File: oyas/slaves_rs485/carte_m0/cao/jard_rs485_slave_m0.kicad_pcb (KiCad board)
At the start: 2 copper layers, 78.6 x 30 mm, 69 parts, among them J1 POWER, J2 Niveaux/Débit, J3 EV1, J4 ISCP, Q1 BPC_FMMT38C, Q2 P03P4L-04, U1 BPC_Alim5V, U2 ATSAMD21G18A-A, U3 MAX3485, U4 AP1117-15

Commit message: Finitions PCB
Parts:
- D9: footprint Package_TO_SOT_SMD:SOT-23 -> bpc:BPC_SOT-23-3_HandSoldering
- Q1: footprint bpc:BPC_SOT-23-3 -> bpc:BPC_SOT-23-3_HandSoldering
- TP3: value H -> High
- TP4: value L -> Low
- TP8: value C -> Cmd
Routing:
- net +3.3V: track 251.3 -> 272.7 mm, vias 9 -> 10
- net POWER_12V: track 27.6 -> 26.6 mm
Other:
- board text added: "0"
- board text added: "Oya"
- board text added: "Pompe"
- board text added: "Slave Oya M0 Rev A / 2026"
- board text removed: "Slave Oya MSP430 Rev B / 2025"

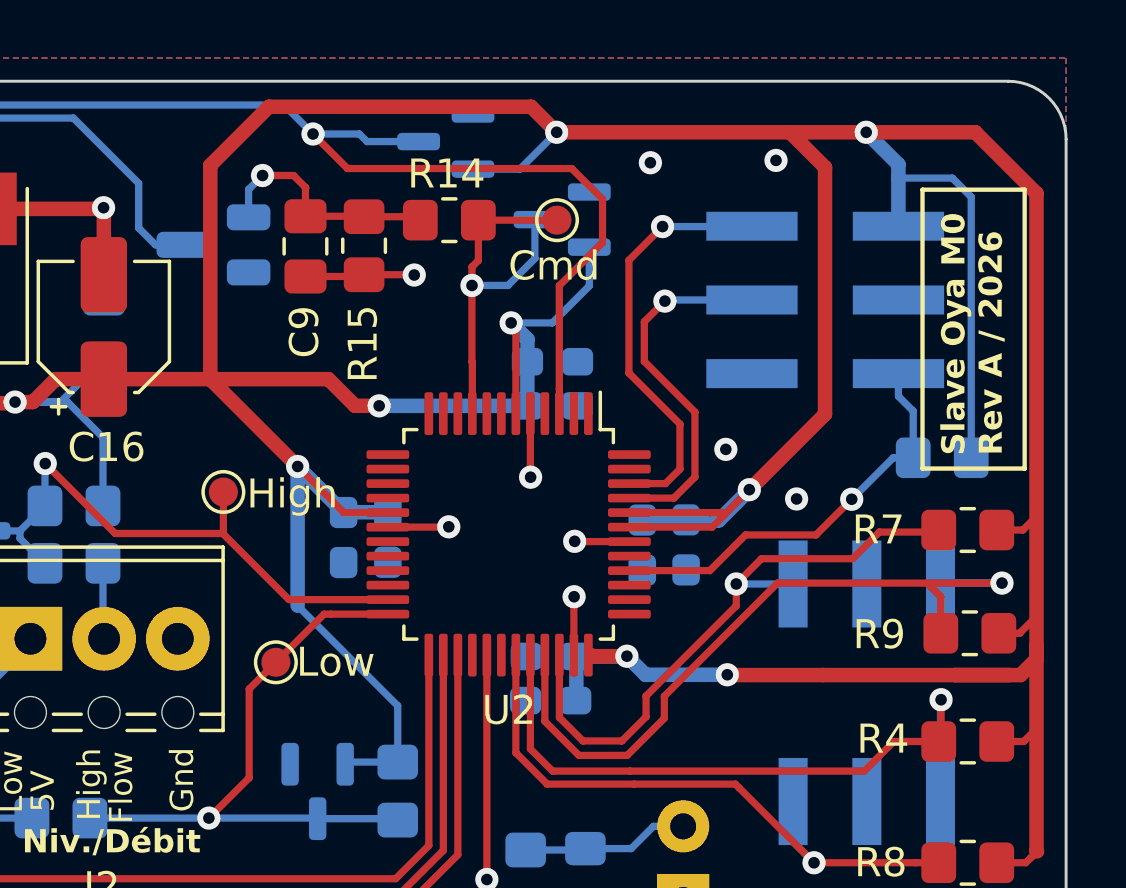
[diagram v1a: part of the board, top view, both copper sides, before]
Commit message: Revue de carte et de routage:
- Amélioration découplage micro (1uF 805 sur VDDCore et 100nF 603 sur les autres selon recommendation microchip)
- R14=1k: Moins de courant dans Q1
- R1=R2=1k: Limiter le clamp en mode débit
- R3 NM en mode débit
- C17=100nF pour améliorer filtrage 3.3V
- Ajout Capa 100nF sur reset
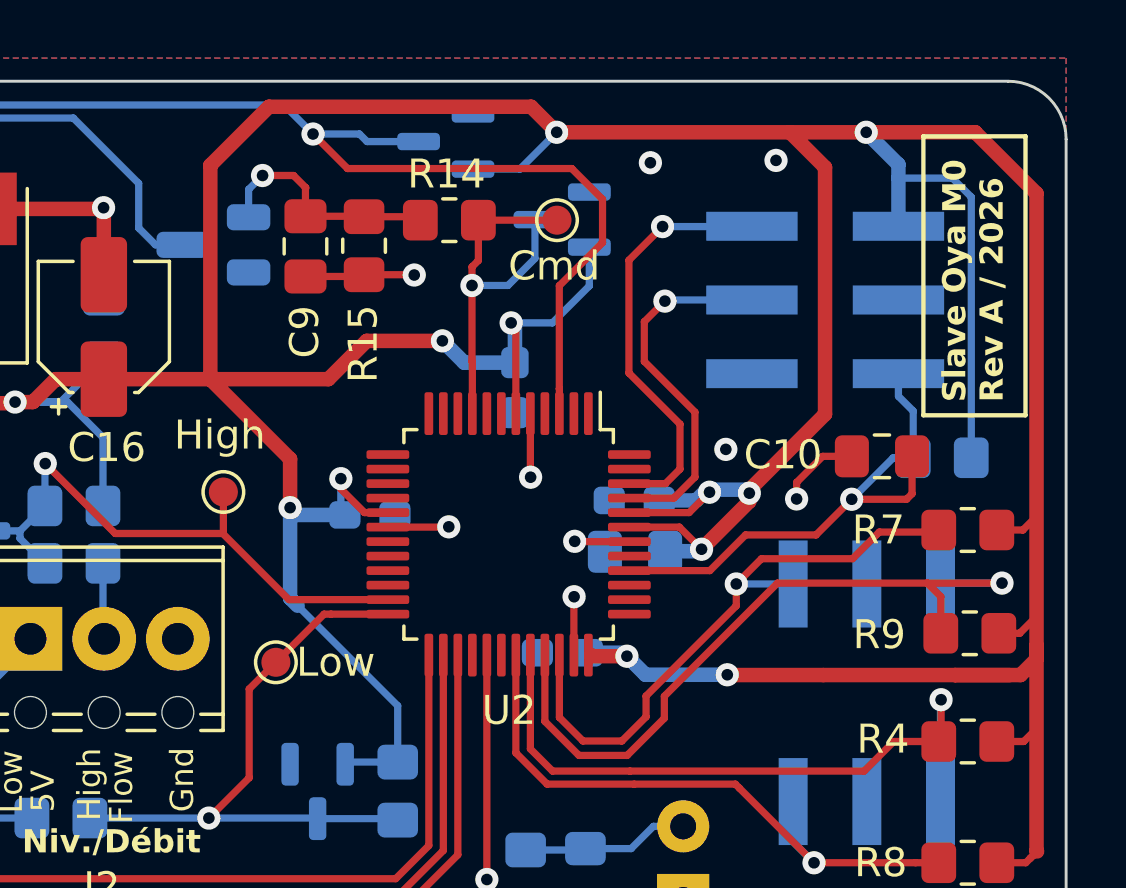
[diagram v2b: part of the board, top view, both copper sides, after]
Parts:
- removed C12: 1µF, Capacitor_SMD:C_0603_1608Metric_Pad1.08x0.95mm_HandSolder
- removed C14: 1nF, Capacitor_SMD:C_0603_1608Metric_Pad1.08x0.95mm_HandSolder
- C10: value 1µF -> 100nF; footprint Capacitor_SMD:C_0603_1608Metric_Pad1.08x0.95mm_HandSolder -> Capacitor_SMD:C_0805_2012Metric_Pad1.18x1.45mm_HandSolder; moved to F.Cu
- C11, C15, C17, C5: value 1nF -> 100nF
- C13: footprint Capacitor_SMD:C_0603_1608Metric_Pad1.08x0.95mm_HandSolder -> Capacitor_SMD:C_0805_2012Metric_Pad1.18x1.45mm_HandSolder
- C4: value 1µF -> 100nF
- R1, R2: value 100 -> 1k
- R14: value 220 -> 1k
- moved C10 17.3 mm to (185.7, 99.7), turned to 0 degrees
- moved C4 4.31 mm to (177.1, 101.2)
- moved C5 1.57 mm to (173.0, 97.4), turned to 90 degrees
- moved C11 1.19 mm to (168.0, 101.8), turned to 180 degrees
- moved C15 0.40 mm to (174.6, 106.5)
- moved C13 0.34 mm to (177.1, 103.0), turned to 180 degrees
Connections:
- C10 pad 2: +3.3V -> /RESET
- C4 pad 1: GND -> +3.3V
- C4 pad 2: +3.3V -> GND
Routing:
- net +3.3V: track 272.7 -> 267.4 mm, vias 10 -> 13
- net /RESET: track 14.5 -> 18.0 mm
- net GND: track 46.8 -> 49.7 mm

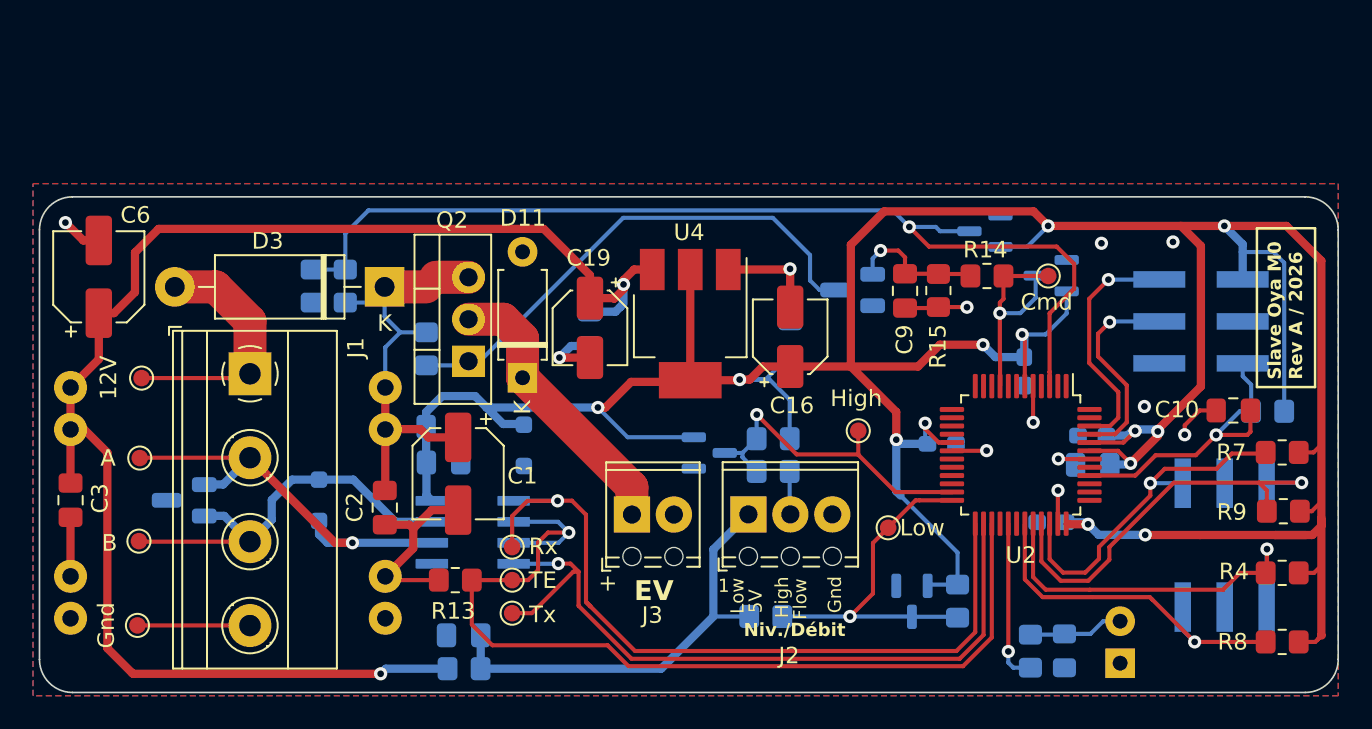
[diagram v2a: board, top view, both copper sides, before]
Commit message: Fin de revue avec ajout d'une diode TVS 18V en entrée
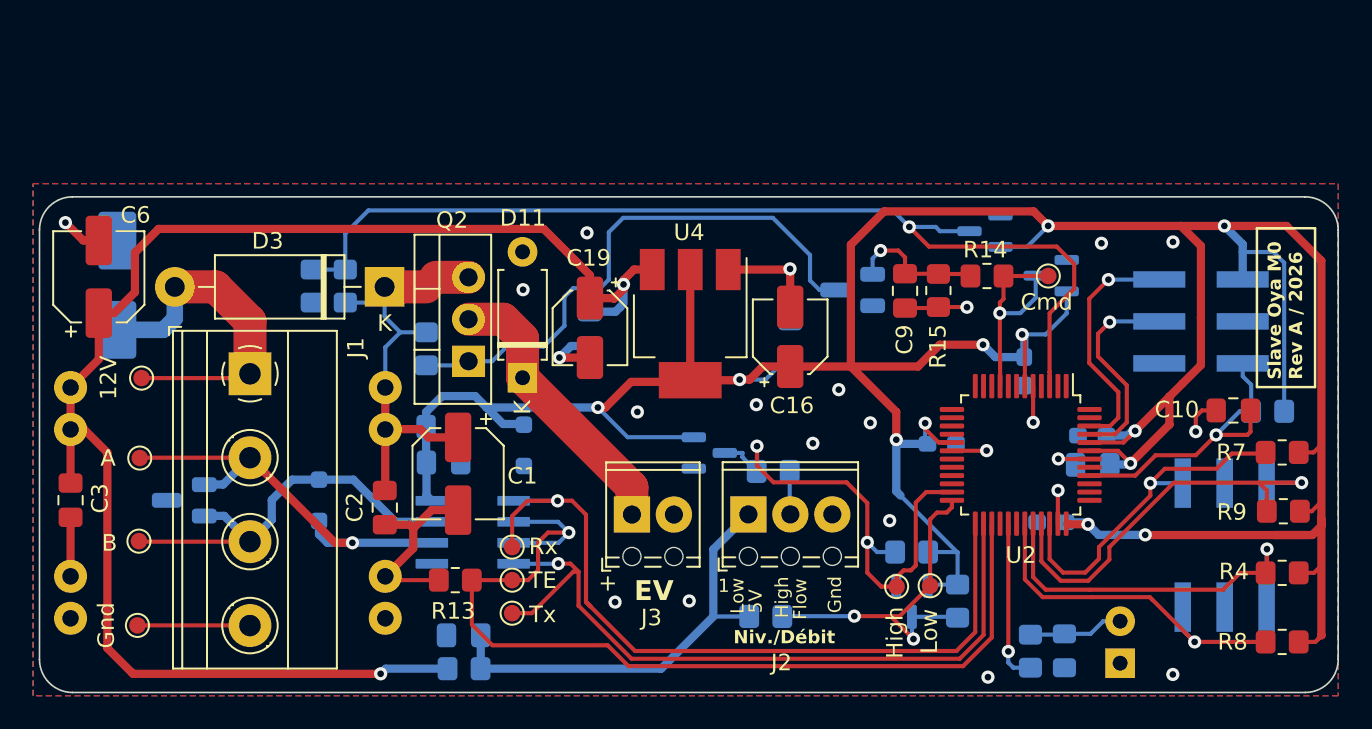
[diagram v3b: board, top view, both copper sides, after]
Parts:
- added D12: SMBJ18A, Diode_SMD:D_SMB_Handsoldering, B.Cu at (118.1, 92.2)
- moved R3 10.8 mm to (166.2, 108.3)
- moved TP3 9.71 mm to (165.3, 110.4)
- moved TP4 4.33 mm to (167.3, 110.3)
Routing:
- net LVL_HIGH_FLOW: track 20.4 -> 29.4 mm, vias 1 -> 2
- net Net-(D12-A1): track 15.3 -> 20.9 mm
- net Net-(Q1-C): track 31.2 -> 33.9 mm
- net +3.3V: track 267.4 -> 264.8 mm, vias 13 -> 12
- net GND: track 49.7 -> 49.1 mm, vias 12 -> 23
- net LVL_LOW: track 21.5 -> 21.9 mm, vias 1 -> 2

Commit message: Préparation future carte Rev B (Inversion TX/RX) Programme en cours de test
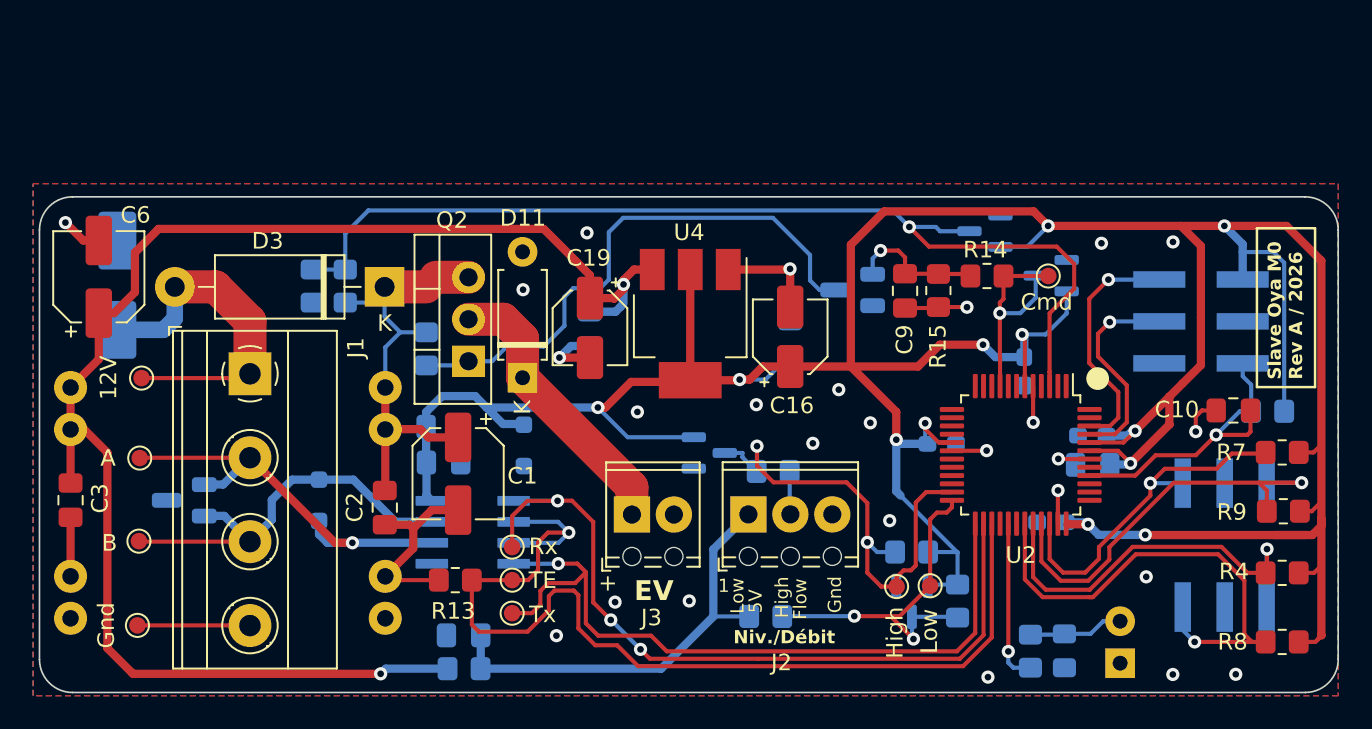
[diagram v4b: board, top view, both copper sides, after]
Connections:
- U2 pad 25: RX -> TX
- U2 pad 26: TX -> RX
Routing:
- net A3: track 21.9 -> 29.7 mm
- net TX_EN: track 58.1 -> 61.8 mm
- net A1: track 23.0 -> 24.3 mm
- net TX: track 44.4 -> 45.0 mm
- net RX: track 47.2 -> 47.6 mm, vias 1 -> 3
- net GND: vias 23 -> 26

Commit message: Amélioration pad de R10 Sortie du module adc Calibration de la mesure d'alim
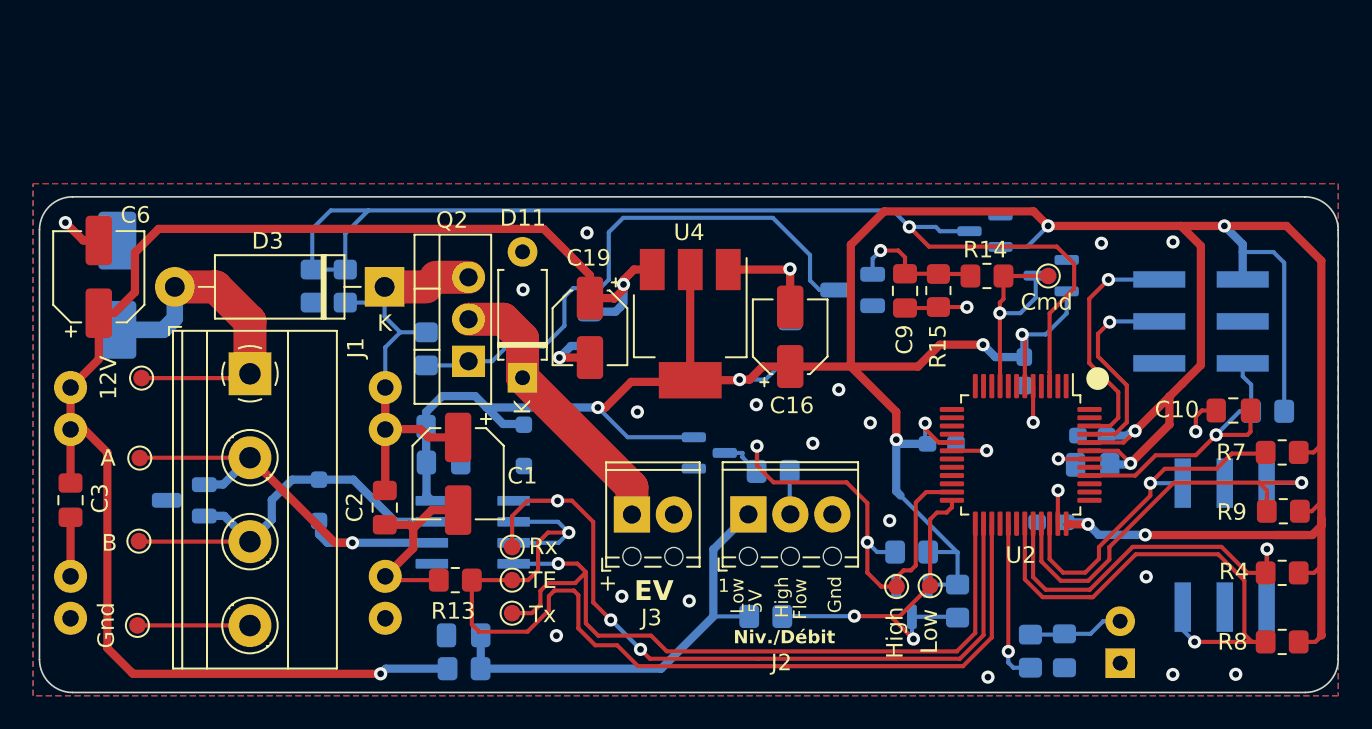
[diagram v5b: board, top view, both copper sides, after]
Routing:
- net POW_MES: track 62.0 -> 68.3 mm
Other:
- board text removed: "Slave Oya M0 Rev A / 2026"
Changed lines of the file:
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@@
   (gr_circle (center 144.06 104.71) (end 143.76 104.74)
     (stroke (width 0.15) (type solid)) (fill solid) (layer "B.SilkS"))
-  (gr_rect (start 148.6 87.95) (end 157.95 91.31)
-    (stroke (width 0.15) (type solid)) (fill none) (layer "B.SilkS"))
   (gr_circle (center 187.76 113.93) (end 188.26 113.93)
     (stroke (width 0.1) (type solid)) (fill solid) (layer "B.SilkS"))
@@
   (gr_line (start 158.35 109.96) (end 158.35 111.22)
     (stroke (width 0.1) (type solid)) (layer "B.SilkS"))
-  (gr_rect (start 187.08 88.7) (end 190.6 98.3154)
-    (stroke (width 0.15) (type solid)) (fill none) (layer "F.SilkS"))
   (gr_circle (center 177.44 97.8) (end 178.052944 97.8)
     (stroke (width 0.15) (type solid)) (fill solid) (layer "F.SilkS"))
@@
   (gr_arc locked (start 190 86.8) (mid 191.414216 87.385784) (end 192 88.8)
     (stroke (width 0.1) (type default)) (layer "Edge.Cuts"))
-  (gr_text "Slave Oya M0\nRev A / 2026" (at 157.6475 90.74) (layer "B.SilkS")
-    (effects (font (size 0.8 0.8) (thickness 0.15) bold) (justify left bottom mirror))
-  )
   (gr_text "Oya" (at 162.25 113.5 180) (layer "B.SilkS")
     (effects (font (size 0.8 0.8) (thickness 0.1)) (justify left bottom mirror))
@@
     (effects (font (size 1.2 1.2) (thickness 0.25) bold) (justify left bottom))
   )
-  (gr_text "Slave Oya M0\nRev A / 2026" (at 189.91 97.8625 90) (layer "F.SilkS")
-    (effects (font (size 0.8 0.8) (thickness 0.15) bold) (justify left bottom))
-  )
   (gr_text "High" (at 158.8 112.3 90) (layer "F.SilkS")
     (effects (font (size 0.8 0.8) (thickness 0.1)) (justify left bottom))
@@
     (effects (font (size 0.8 0.8) (thickness 0.16) bold) (justify left bottom))
   )
+  (gr_text_box "Slave Oya m0\nRev B / 2026"
+    (start 157.91 91.37) (end 147.55 87.76) (angle 180) (layer "B.SilkS")
+      (effects (font (size 0.8 0.8) (thickness 0.2) bold) (justify top mirror))
+    (stroke (width 0.2) (type solid))  )
+  (gr_text_box "Slave Oya m0\nRev B / 2026"
+    (start 180.39 90.36) (end 190.75 93.97) (angle 360) (layer "F.SilkS")
+      (effects (font (size 0.8 0.8) (thickness 0.2) bold) (justify top))
+    (stroke (width 0.2) (type solid))  )
   (segment (start 173.5325 98.2575) (end 173.5325 100.4425) (width 0.25) (layer "F.Cu") (net 1))
   (segment (start 169.52 93.47) (end 169.53 93.48) (width 0.25) (layer "F.Cu") (net 1))
@@
   (via (at 173.54 100.45) (size 0.8) (drill 0.4) (layers "F.Cu" "B.Cu") (net 1))
   (via (at 144.68 113.36) (size 0.8) (drill 0.4) (layers "F.Cu" "B.Cu") (free) (net 1))
-  (via (at 148.23 111.33) (size 0.8) (drill 0.4) (layers "F.Cu" "B.Cu") (free) (net 1))
+  (via (at 148.64 110.98) (size 0.8) (drill 0.4) (layers "F.Cu" "B.Cu") (free) (net 1))
   (via (at 164.85 106.4) (size 0.8) (drill 0.4) (layers "F.Cu" "B.Cu") (free) (net 1))
   (via (at 177.67 89.61) (size 0.8) (drill 0.4) (layers "F.Cu" "B.Cu") (free) (net 1))
@@
   (via (at 166.04 88.62) (size 0.8) (drill 0.4) (layers "F.Cu" "B.Cu") (net 7))
   (segment (start 165.04 87.62) (end 166.04 88.62) (width 0.25) (layer "B.Cu") (net 7))
+  (segment (start 129.9 88.74) (end 131.02 87.62) (width 0.25) (layer "B.Cu") (net 7))
   (segment (start 133.3 87.62) (end 165.04 87.62) (width 0.25) (layer "B.Cu") (net 7))
   (segment (start 167.64 88.62) (end 167.9 88.88) (width 0.25) (layer "B.Cu") (net 7))
   (segment (start 129.9 91.2) (end 131.9 91.2) (width 0.25) (layer "B.Cu") (net 7))
+  (segment (start 129.9 91.2) (end 129.9 88.74) (width 0.25) (layer "B.Cu") (net 7))
   (segment (start 131.9 91.2) (end 131.9 89.02) (width 0.25) (layer "B.Cu") (net 7))
   (segment (start 169.68 88.88) (end 167.9 88.88) (width 0.25) (layer "B.Cu") (net 7))
+  (segment (start 131.02 87.62) (end 133.3 87.62) (width 0.25) (layer "B.Cu") (net 7))
   (segment (start 166.04 88.62) (end 167.64 88.62) (width 0.25) (layer "B.Cu") (net 7))
   (segment (start 131.9 89.02) (end 133.3 87.62) (width 0.25) (layer "B.Cu") (net 7))

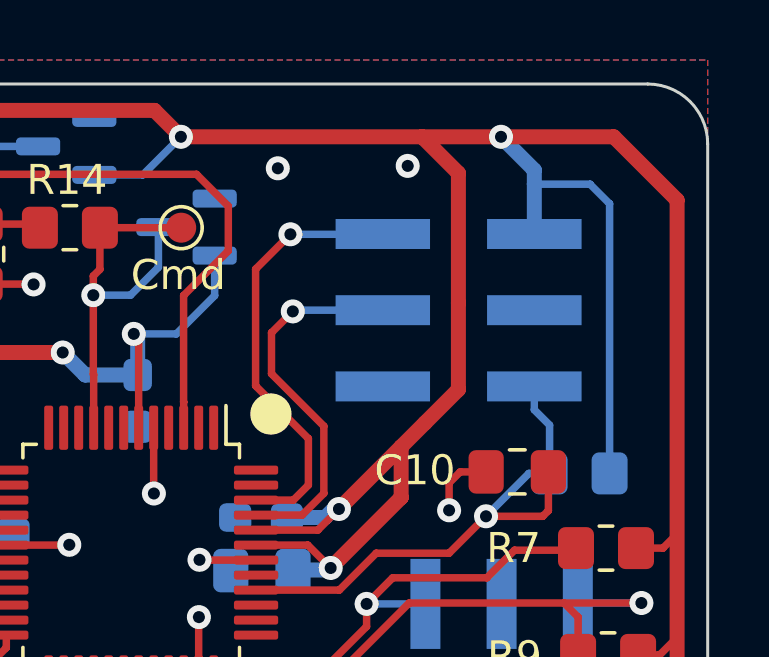
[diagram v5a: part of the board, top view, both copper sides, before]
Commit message: Changement connecteur de programmation
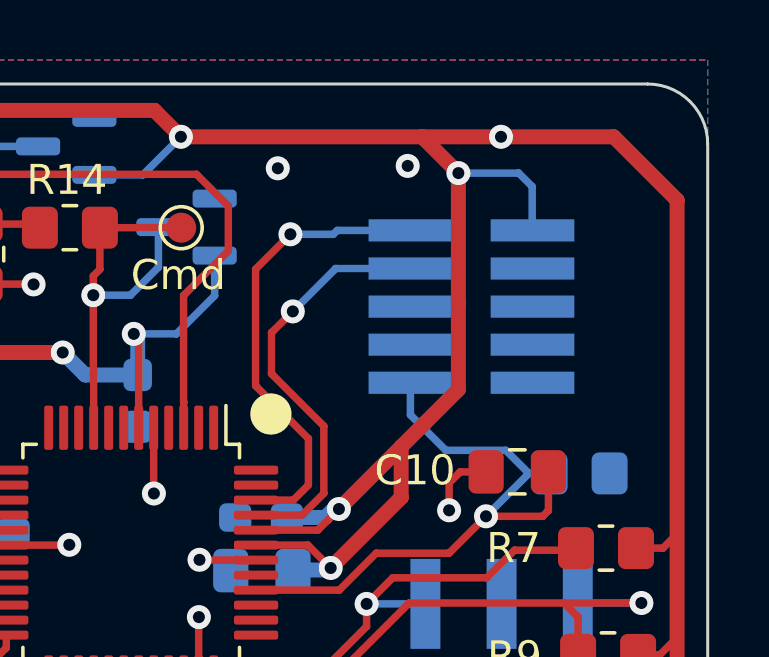
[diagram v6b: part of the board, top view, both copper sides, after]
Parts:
- removed J4: ISCP, bpc:BPC_ISCP_CMS
- added J5: BPC_PRG_FTSH-105-01-L-DV-K_1, bpc:BPC_SAMTEC_FTSH-105-01-L-DV-K, B.Cu at (184.1, 94.2)
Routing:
- net +3.3V: track 264.8 -> 253.4 mm, vias 12 -> 13
- net /RESET: track 18.0 -> 20.7 mm
- net SWCLK: track 12.7 -> 14.2 mm
- net SWDIO: track 14.6 -> 15.6 mm
